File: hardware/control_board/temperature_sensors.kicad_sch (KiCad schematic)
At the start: 23 parts, among them J5 RTD, J5 TC, U2 MAX6675, U6 MCP6N11T-005E, U7 MCP6001T

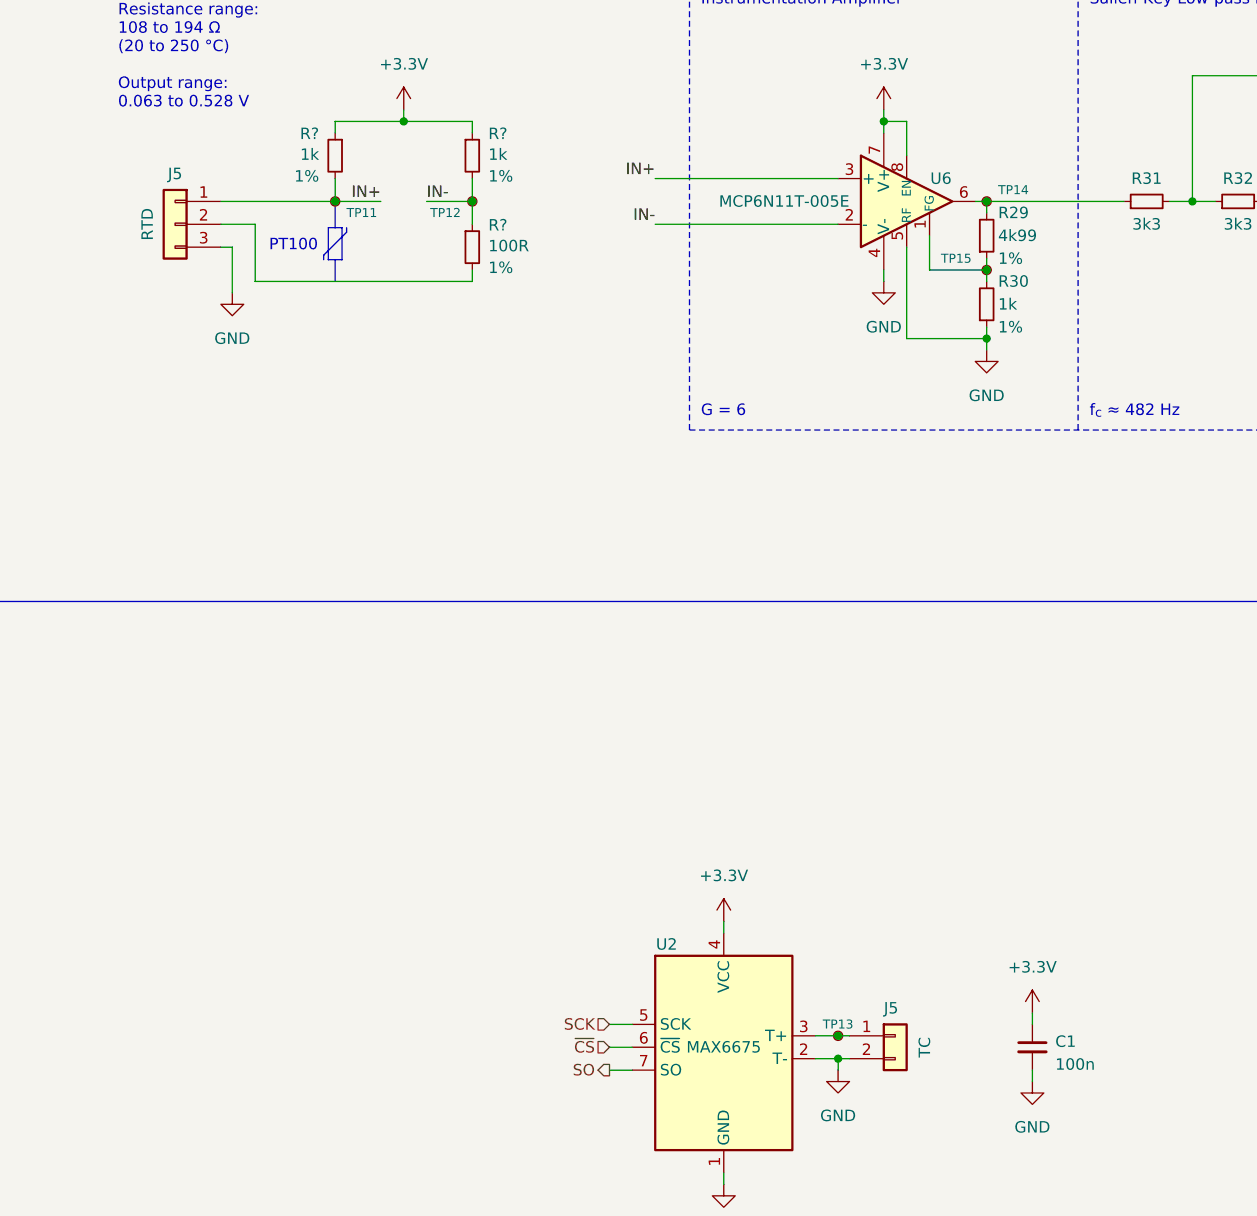
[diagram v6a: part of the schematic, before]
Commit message: Update reference designators
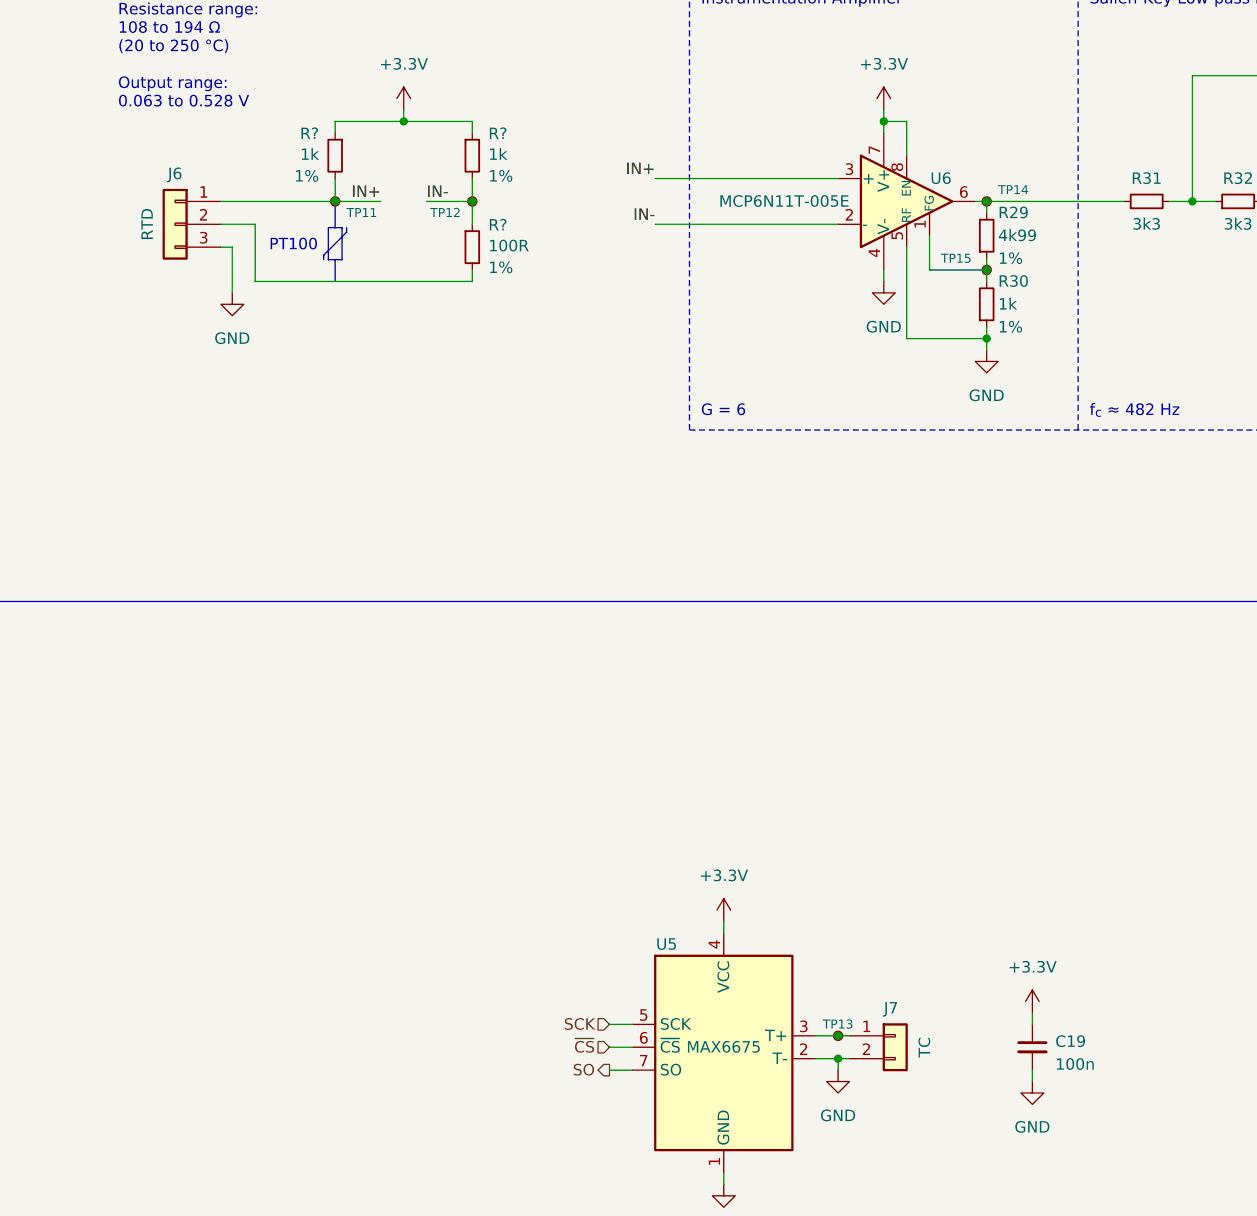
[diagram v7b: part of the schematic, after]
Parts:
- renumbered C1 to C19, J5 to J6, J5 to J7, U2 to U5
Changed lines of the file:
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@@
   (symbol (lib_id "power:GND") (at 116.84 167.64 0) (unit 1)
     (in_bom yes) (on_board yes) (dnp no)
-    (property "Reference" "#PWR09" (at 116.84 173.99 0)
+    (property "Reference" "#PWR065" (at 116.84 173.99 0)
       (effects (font (size 1.27 1.27)) hide)
     )
@@
     (instances
       (project "control_board"
-        (path "/82fde900-07e6-41de-9b57-509c777c8289"
-          (reference "#PWR09") (unit 1)
-        )
-      )
-      (project "control_board"
-        (path "/b652b05a-4e3d-4ad1-b032-18886abe7d45"
-          (reference "#PWR03") (unit 1)
-        )
         (path "/b652b05a-4e3d-4ad1-b032-18886abe7d45/02711725-e382-48ba-bf33-23fe46c66e66"
           (reference "#PWR065") (unit 1)
-        )
-        (path "/b652b05a-4e3d-4ad1-b032-18886abe7d45/d341d3a2-ea4e-4772-851c-7c5b5be32855"
-          (reference "#PWR021") (unit 1)
         )
       )
@@
   (symbol (lib_id "power:+3.3V") (at 116.84 138.43 0) (unit 1)
     (in_bom yes) (on_board yes) (dnp no)
-    (property "Reference" "#PWR015" (at 116.84 142.24 0)
+    (property "Reference" "#PWR064" (at 116.84 142.24 0)
       (effects (font (size 1.27 1.27)) hide)
     )
@@
     (instances
       (project "control_board"
-        (path "/b652b05a-4e3d-4ad1-b032-18886abe7d45"
-          (reference "#PWR015") (unit 1)
-        )
         (path "/b652b05a-4e3d-4ad1-b032-18886abe7d45/02711725-e382-48ba-bf33-23fe46c66e66"
           (reference "#PWR064") (unit 1)
@@
   (symbol (lib_id "power:GND") (at 151.13 156.21 0) (unit 1)
     (in_bom yes) (on_board yes) (dnp no)
-    (property "Reference" "#PWR09" (at 151.13 162.56 0)
+    (property "Reference" "#PWR071" (at 151.13 162.56 0)
       (effects (font (size 1.27 1.27)) hide)
     )
@@
     (instances
       (project "control_board"
-        (path "/82fde900-07e6-41de-9b57-509c777c8289"
-          (reference "#PWR09") (unit 1)
-        )
-      )
-      (project "control_board"
-        (path "/b652b05a-4e3d-4ad1-b032-18886abe7d45"
-          (reference "#PWR08") (unit 1)
-        )
         (path "/b652b05a-4e3d-4ad1-b032-18886abe7d45/02711725-e382-48ba-bf33-23fe46c66e66"
           (reference "#PWR071") (unit 1)
         )
-        (path "/b652b05a-4e3d-4ad1-b032-18886abe7d45/d341d3a2-ea4e-4772-851c-7c5b5be32855"
-          (reference "#PWR018") (unit 1)
-        )
       )
     )
@@
   (symbol (lib_id "power:+3.3V") (at 134.62 48.26 0) (unit 1)
     (in_bom yes) (on_board yes) (dnp no)
-    (property "Reference" "#PWR015" (at 134.62 52.07 0)
+    (property "Reference" "#PWR067" (at 134.62 52.07 0)
       (effects (font (size 1.27 1.27)) hide)
     )
@@
     (instances
       (project "control_board"
-        (path "/b652b05a-4e3d-4ad1-b032-18886abe7d45"
-          (reference "#PWR015") (unit 1)
-        )
         (path "/b652b05a-4e3d-4ad1-b032-18886abe7d45/02711725-e382-48ba-bf33-23fe46c66e66"
           (reference "#PWR067") (unit 1)
@@
   (symbol (lib_id "MAX6675:MAX6675") (at 116.84 152.4 0) (unit 1)
     (in_bom yes) (on_board yes) (dnp no)
-    (property "Reference" "U2" (at 110.49 140.97 0)
+    (property "Reference" "U5" (at 110.49 140.97 0)
       (effects (font (size 1.27 1.27)))
     )
@@
     (instances
       (project "control_board"
-        (path "/82fde900-07e6-41de-9b57-509c777c8289"
-          (reference "U2") (unit 1)
-        )
-      )
-      (project "control_board"
-        (path "/b652b05a-4e3d-4ad1-b032-18886abe7d45"
-          (reference "U2") (unit 1)
-        )
         (path "/b652b05a-4e3d-4ad1-b032-18886abe7d45/02711725-e382-48ba-bf33-23fe46c66e66"
           (reference "U5") (unit 1)
         )
-        (path "/b652b05a-4e3d-4ad1-b032-18886abe7d45/d341d3a2-ea4e-4772-851c-7c5b5be32855"
-          (reference "U4") (unit 1)
-        )
       )
     )
@@
   (symbol (lib_id "power:+3.3V") (at 81.28 48.26 0) (unit 1)
     (in_bom yes) (on_board yes) (dnp no)
-    (property "Reference" "#PWR015" (at 81.28 52.07 0)
+    (property "Reference" "#PWR063" (at 81.28 52.07 0)
       (effects (font (size 1.27 1.27)) hide)
     )
@@
     (instances
       (project "control_board"
-        (path "/b652b05a-4e3d-4ad1-b032-18886abe7d45"
-          (reference "#PWR015") (unit 1)
-        )
         (path "/b652b05a-4e3d-4ad1-b032-18886abe7d45/02711725-e382-48ba-bf33-23fe46c66e66"
           (reference "#PWR063") (unit 1)
@@
   (symbol (lib_id "power:+3.3V") (at 241.3 55.88 0) (unit 1)
     (in_bom yes) (on_board yes) (dnp no)
-    (property "Reference" "#PWR015" (at 241.3 59.69 0)
+    (property "Reference" "#PWR075" (at 241.3 59.69 0)
       (effects (font (size 1.27 1.27)) hide)
     )
@@
     (instances
       (project "control_board"
-        (path "/b652b05a-4e3d-4ad1-b032-18886abe7d45"
-          (reference "#PWR015") (unit 1)
-        )
         (path "/b652b05a-4e3d-4ad1-b032-18886abe7d45/02711725-e382-48ba-bf33-23fe46c66e66"
           (reference "#PWR075") (unit 1)
@@
   (symbol (lib_id "Connector_Generic:Conn_01x03") (at 55.88 60.96 0) (mirror y) (unit 1)
     (in_bom yes) (on_board yes) (dnp no)
-    (property "Reference" "J5" (at 55.88 54.61 0)
+    (property "Reference" "J6" (at 55.88 54.61 0)
       (effects (font (size 1.27 1.27)) (justify top))
     )
@@
     (instances
       (project "control_board"
-        (path "/82fde900-07e6-41de-9b57-509c777c8289"
-          (reference "J5") (unit 1)
-        )
-      )
-      (project "control_board"
-        (path "/b652b05a-4e3d-4ad1-b032-18886abe7d45"
+        (path "/b652b05a-4e3d-4ad1-b032-18886abe7d45/02711725-e382-48ba-bf33-23fe46c66e66"
           (reference "J6") (unit 1)
         )
-        (path "/b652b05a-4e3d-4ad1-b032-18886abe7d45/02711725-e382-48ba-bf33-23fe46c66e66"
-          (reference "J6") (unit 1)
-        )
-        (path "/b652b05a-4e3d-4ad1-b032-18886abe7d45/d341d3a2-ea4e-4772-851c-7c5b5be32855"
-          (reference "J8") (unit 1)
-        )
       )
     )
@@
   (symbol (lib_id "power:GND") (at 129.54 154.94 0) (unit 1)
     (in_bom yes) (on_board yes) (dnp no)
-    (property "Reference" "#PWR09" (at 129.54 161.29 0)
+    (property "Reference" "#PWR066" (at 129.54 161.29 0)
       (effects (font (size 1.27 1.27)) hide)
     )
@@
     (instances
       (project "control_board"
-        (path "/82fde900-07e6-41de-9b57-509c777c8289"
-          (reference "#PWR09") (unit 1)
-        )
-      )
-      (project "control_board"
-        (path "/b652b05a-4e3d-4ad1-b032-18886abe7d45"
-          (reference "#PWR02") (unit 1)
-        )
         (path "/b652b05a-4e3d-4ad1-b032-18886abe7d45/02711725-e382-48ba-bf33-23fe46c66e66"
           (reference "#PWR066") (unit 1)
-        )
-        (path "/b652b05a-4e3d-4ad1-b032-18886abe7d45/d341d3a2-ea4e-4772-851c-7c5b5be32855"
-          (reference "#PWR022") (unit 1)
         )
       )
@@
   (symbol (lib_id "power:+3.3V") (at 151.13 148.59 0) (unit 1)
     (in_bom yes) (on_board yes) (dnp no)
-    (property "Reference" "#PWR015" (at 151.13 152.4 0)
+    (property "Reference" "#PWR070" (at 151.13 152.4 0)
       (effects (font (size 1.27 1.27)) hide)
     )
@@
     (instances
       (project "control_board"
-        (path "/b652b05a-4e3d-4ad1-b032-18886abe7d45"
-          (reference "#PWR015") (unit 1)
-        )
         (path "/b652b05a-4e3d-4ad1-b032-18886abe7d45/02711725-e382-48ba-bf33-23fe46c66e66"
           (reference "#PWR070") (unit 1)
@@
   (symbol (lib_id "Device:C_Small") (at 151.13 152.4 0) (unit 1)
     (in_bom yes) (on_board yes) (dnp no)
-    (property "Reference" "C1" (at 153.67 151.7713 0)
+    (property "Reference" "C19" (at 153.67 151.7713 0)
       (effects (font (size 1.27 1.27)) (justify left))
     )
@@
     (instances
       (project "control_board"
-        (path "/82fde900-07e6-41de-9b57-509c777c8289"
-          (reference "C1") (unit 1)
-        )
-      )
-      (project "control_board"
-        (path "/b652b05a-4e3d-4ad1-b032-18886abe7d45"
-          (reference "C1") (unit 1)
-        )
         (path "/b652b05a-4e3d-4ad1-b032-18886abe7d45/02711725-e382-48ba-bf33-23fe46c66e66"
           (reference "C19") (unit 1)
         )
-        (path "/b652b05a-4e3d-4ad1-b032-18886abe7d45/d341d3a2-ea4e-4772-851c-7c5b5be32855"
-          (reference "C2") (unit 1)
-        )
       )
     )
@@
   (symbol (lib_id "power:+3.3V") (at 199.39 52.07 0) (unit 1)
     (in_bom yes) (on_board yes) (dnp no)
-    (property "Reference" "#PWR015" (at 199.39 55.88 0)
+    (property "Reference" "#PWR073" (at 199.39 55.88 0)
       (effects (font (size 1.27 1.27)) hide)
     )
@@
     (instances
       (project "control_board"
-        (path "/b652b05a-4e3d-4ad1-b032-18886abe7d45"
-          (reference "#PWR015") (unit 1)
-        )
         (path "/b652b05a-4e3d-4ad1-b032-18886abe7d45/02711725-e382-48ba-bf33-23fe46c66e66"
           (reference "#PWR073") (unit 1)
@@
   (symbol (lib_id "Connector_Generic:Conn_01x02") (at 135.89 151.13 0) (unit 1)
     (in_bom yes) (on_board yes) (dnp no)
-    (property "Reference" "J5" (at 134.62 147.32 0)
+    (property "Reference" "J7" (at 134.62 147.32 0)
       (effects (font (size 1.27 1.27)) (justify left top))
     )
@@
     (instances
       (project "control_board"
-        (path "/82fde900-07e6-41de-9b57-509c777c8289"
-          (reference "J5") (unit 1)
-        )
-      )
-      (project "control_board"
-        (path "/b652b05a-4e3d-4ad1-b032-18886abe7d45"
-          (reference "J6") (unit 1)
-        )
         (path "/b652b05a-4e3d-4ad1-b032-18886abe7d45/02711725-e382-48ba-bf33-23fe46c66e66"
           (reference "J7") (unit 1)
         )
-        (path "/b652b05a-4e3d-4ad1-b032-18886abe7d45/d341d3a2-ea4e-4772-851c-7c5b5be32855"
-          (reference "J8") (unit 1)
-        )
-      )
+      )
